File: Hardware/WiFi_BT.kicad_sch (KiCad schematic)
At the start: 6 parts, among them J5 Conn_01x12, U7 ESP32-S3-WROOM-1

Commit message: First modification for v2
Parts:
- added P1: ESP_DATA, Connector_USB:USB_C_Receptacle_Palconn_UTC16-G, symbol Connector:USB_C_Receptacle_USB2.0
- added R10, R13: 10k, Resistor_SMD:R_0402_1005Metric, symbol Device:R
- added SW5: ESP_BOOT, TS-1184:TS-1187A-B-A-B, symbol Switch:SW_DIP_x01
- added SW6: ESP_RST, TS-1184:TS-1187A-B-A-B, symbol Switch:SW_DIP_x01
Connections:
- net +3V3: now also R10.1, R13.1
- net GND: now also P1.A1 (GND), P1.A12 (GND), P1.B1 (GND), P1.B12 (GND), P1.S1 (SHIELD), SW5.1, SW6.1
- net IO43: no longer names the net of J5.15 (Pin_15)
- net IO43: no longer U7.14 (GPIO20/U1CTS/ADC2_CH9/CLK_OUT1/USB_D+)
- net IO44: no longer names the net of J5.17 (Pin_17)
- net IO44: no longer U7.13 (GPIO19/U1RTS/ADC2_CH8/CLK_OUT2/USB_D-)
- new net: P1.A4 (VBUS), P1.A9 (VBUS), P1.B4 (VBUS), P1.B9 (VBUS)
- new net ESP_BOOT: R10.2, SW5.2
- new net ESP_EN: R13.2, SW6.2
- new net ESP_USB+: P1.A6 (D+), P1.B6 (D+), U7.14 (GPIO20/U1CTS/ADC2_CH9/CLK_OUT1/USB_D+)
- new net ESP_USB-: P1.A7 (D-), P1.B7 (D-), U7.13 (GPIO19/U1RTS/ADC2_CH8/CLK_OUT2/USB_D-)

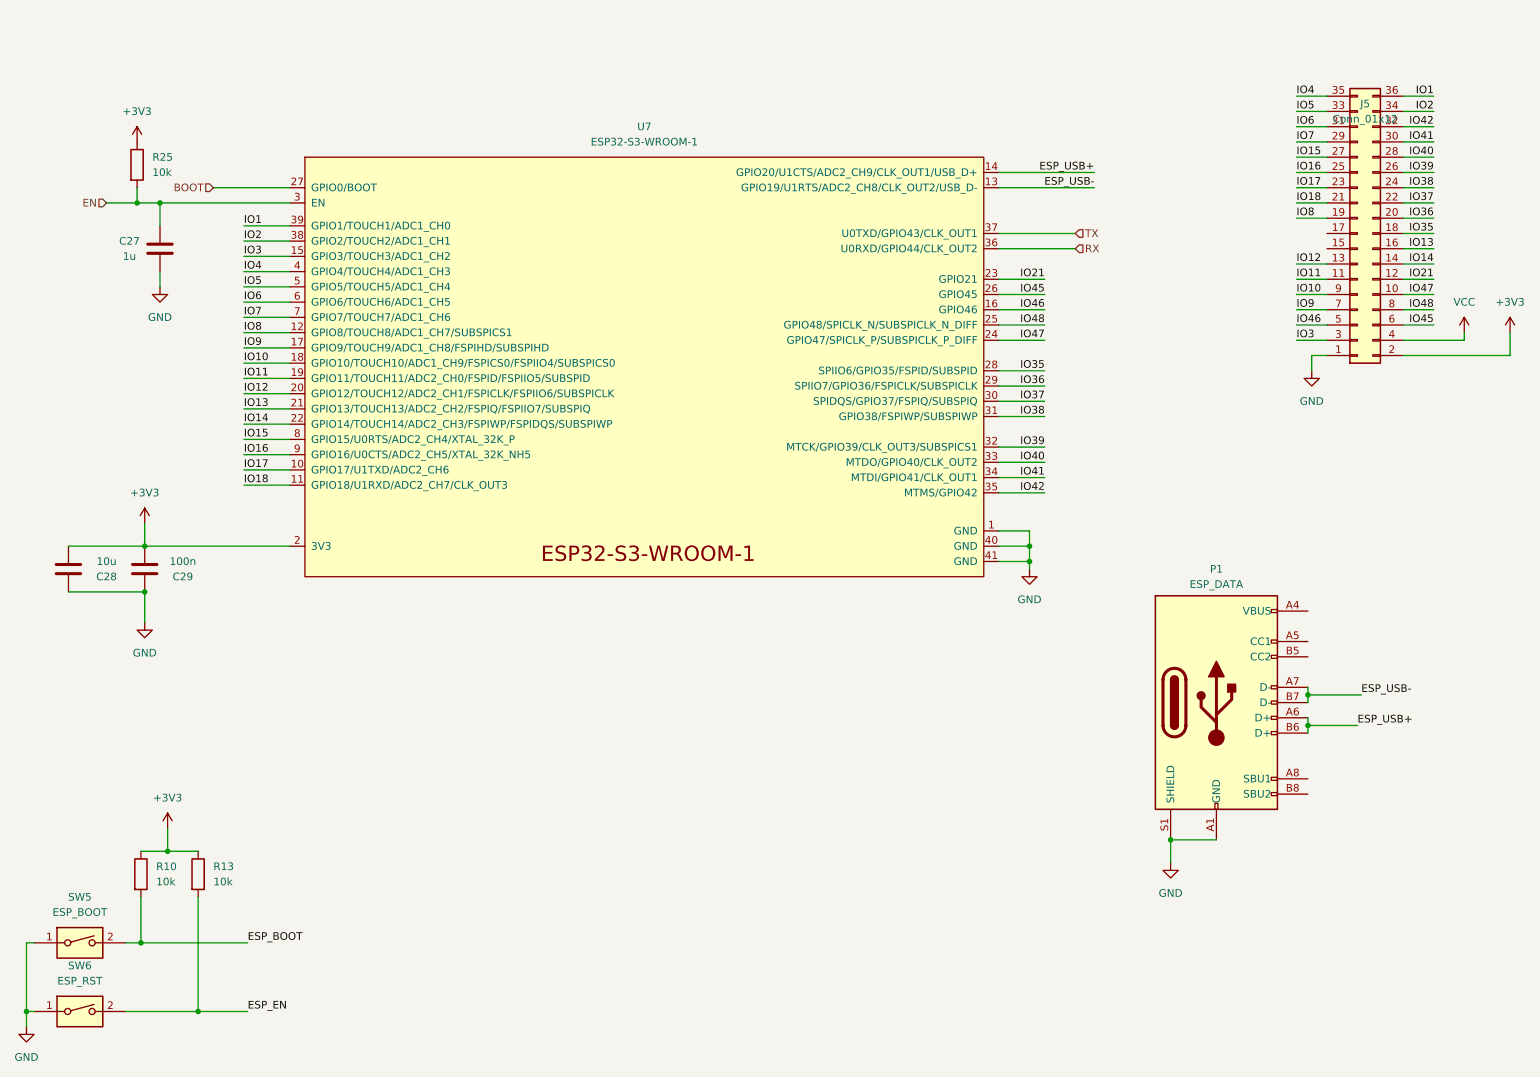
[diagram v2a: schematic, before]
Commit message: WIP - Added NFC Antenna and connected almost everythings else
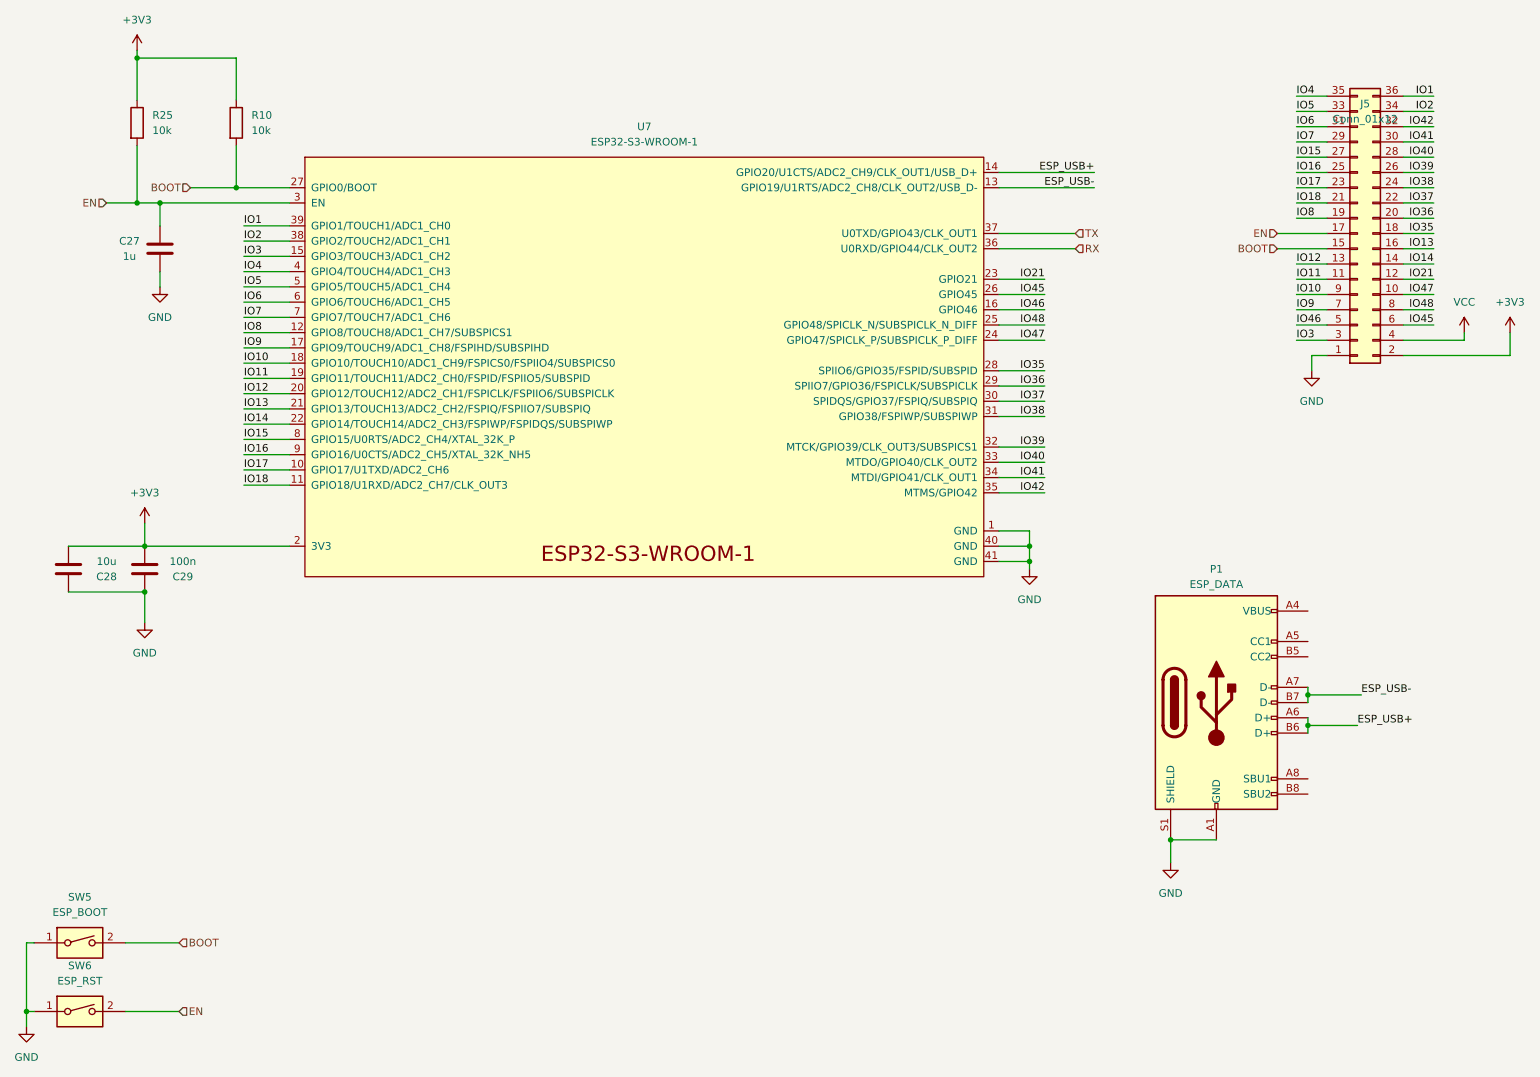
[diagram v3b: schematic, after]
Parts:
- removed R13: 10k, Resistor_SMD:R_0402_1005Metric, symbol Device:R
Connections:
- net ESP_BOOT is gone; now on net BOOT: R10.2, SW5.2
- net ESP_EN is gone; now on net EN: SW6.2
- net BOOT: now also J5.15 (Pin_15)
- net EN: now also J5.17 (Pin_17)
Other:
- moved on the sheet: R25

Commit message: All upgrade done, start working on lesser stuff (like silkscreen)
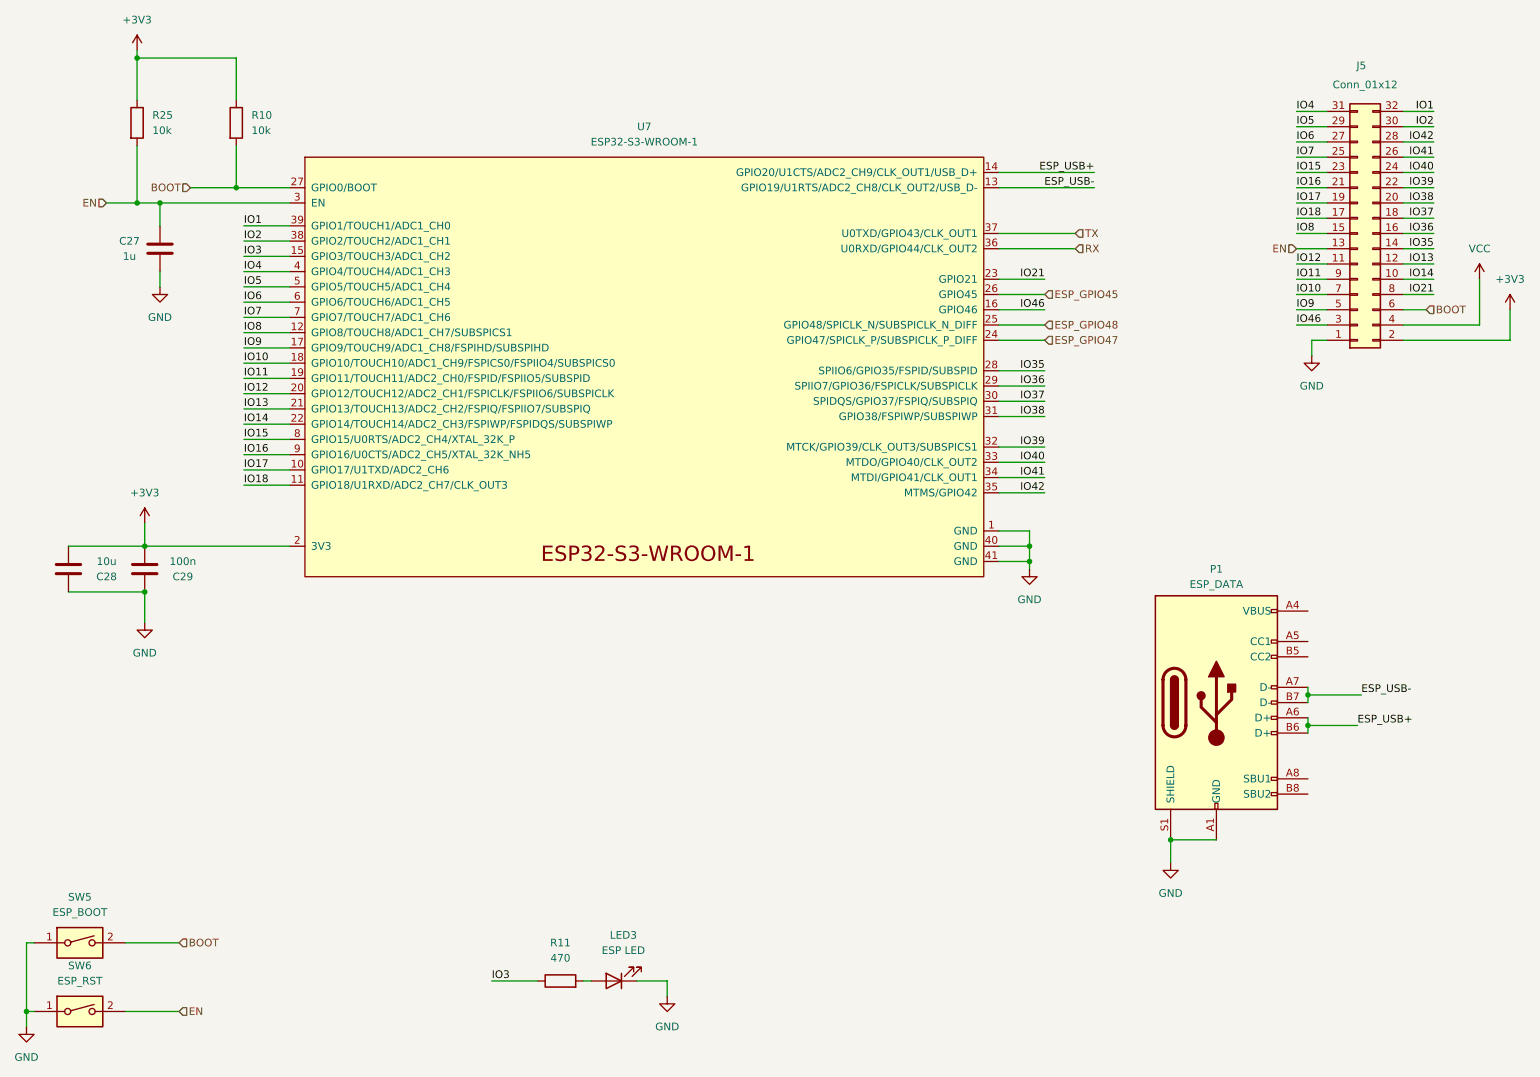
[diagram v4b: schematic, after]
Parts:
- added LED3: ESP LED, LED_SMD:LED_0603_1608Metric, symbol Device:LED
- added R11: 470, Resistor_SMD:R_0402_1005Metric, symbol Device:R
- J5: footprint Connector_PinSocket_1.27mm:PinSocket_2x18_P1.27mm_Vertical -> Connector_PinSocket_1.27mm:PinSocket_2x17_P1.27mm_Vertical; symbol Connector_Generic:Conn_02x18_Odd_Even -> Connector_Generic:Conn_02x16_Odd_Even
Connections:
- net BOOT: now also J5.6 (Pin_6); no longer J5.15 (Pin_15)
- net EN: now also J5.13 (Pin_13); no longer J5.17 (Pin_17)
- net GND: now also LED3.1 (K)
- net IO1: now also J5.32 (Pin_32); no longer J5.36 (Pin_36)
- net IO10: now also J5.7 (Pin_7); no longer J5.9 (Pin_9)
- net IO11: now also J5.9 (Pin_9); no longer J5.11 (Pin_11)
- net IO12: now also J5.11 (Pin_11); no longer J5.13 (Pin_13)
- net IO13: now also J5.12 (Pin_12); no longer J5.16 (Pin_16)
- net IO14: now also J5.10 (Pin_10); no longer J5.14 (Pin_14)
- net IO15: now also J5.23 (Pin_23); no longer J5.27 (Pin_27)
- net IO16: now also J5.21 (Pin_21); no longer J5.25 (Pin_25)
- net IO17: now also J5.19 (Pin_19); no longer J5.23 (Pin_23)
- net IO18: now also J5.17 (Pin_17); no longer J5.21 (Pin_21)
- net IO2: now also J5.30 (Pin_30); no longer J5.34 (Pin_34)
- net IO21: now also J5.8 (Pin_8); no longer J5.12 (Pin_12)
- net IO3: now also R11.1; no longer J5.3 (Pin_3)
- net IO35: now also J5.14 (Pin_14); no longer J5.18 (Pin_18)
- net IO36: now also J5.16 (Pin_16); no longer J5.20 (Pin_20)
- net IO37: now also J5.18 (Pin_18); no longer J5.22 (Pin_22)
- net IO38: now also J5.20 (Pin_20); no longer J5.24 (Pin_24)
- net IO39: now also J5.22 (Pin_22); no longer J5.26 (Pin_26)
- net IO4: now also J5.31 (Pin_31); no longer J5.35 (Pin_35)
- net IO40: now also J5.24 (Pin_24); no longer J5.28 (Pin_28)
- net IO41: now also J5.26 (Pin_26); no longer J5.30 (Pin_30)
- net IO42: now also J5.28 (Pin_28); no longer J5.32 (Pin_32)
- net IO46: now also J5.3 (Pin_3); no longer J5.5 (Pin_5)
- net IO5: now also J5.29 (Pin_29); no longer J5.33 (Pin_33)
- net IO6: now also J5.27 (Pin_27); no longer J5.31 (Pin_31)
- net IO7: now also J5.25 (Pin_25); no longer J5.29 (Pin_29)
- net IO8: now also J5.15 (Pin_15); no longer J5.19 (Pin_19)
- net IO9: now also J5.5 (Pin_5); no longer J5.7 (Pin_7)
- net IO45 renamed ESP_GPIO45
- net ESP_GPIO45: no longer J5.6 (Pin_6)
- net IO47 renamed ESP_GPIO47
- net ESP_GPIO47: no longer J5.10 (Pin_10)
- net IO48 renamed ESP_GPIO48
- net ESP_GPIO48: no longer J5.8 (Pin_8)
- new net: LED3.2 (A), R11.2
